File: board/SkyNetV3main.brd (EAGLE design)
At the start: 38 x 67 mm, 61 parts, among them IC1 HC_05, IC2 RF4463PRO, IC3 LPC1768, IC4 BCX17, IC5 TPS63001, IC6 MCP73871-2CCI/ML, Q1 32.768KHz, Q2 12MHz, Q3 IRLM6402, Q4 BSS138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

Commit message: corrected some distance problems and missing VALUEs
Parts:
- IC3: value LPC1768 -> LPC1769
- JP4: value (none) -> EXT
- SJ1: value (none) -> MEASURE
- moved U$1 0.28 mm to (27.5, 3.63)
- moved IC2 0.25 mm to (29.6, 14.8)
- moved JP4 0.10 mm to (34.4, 55.1)

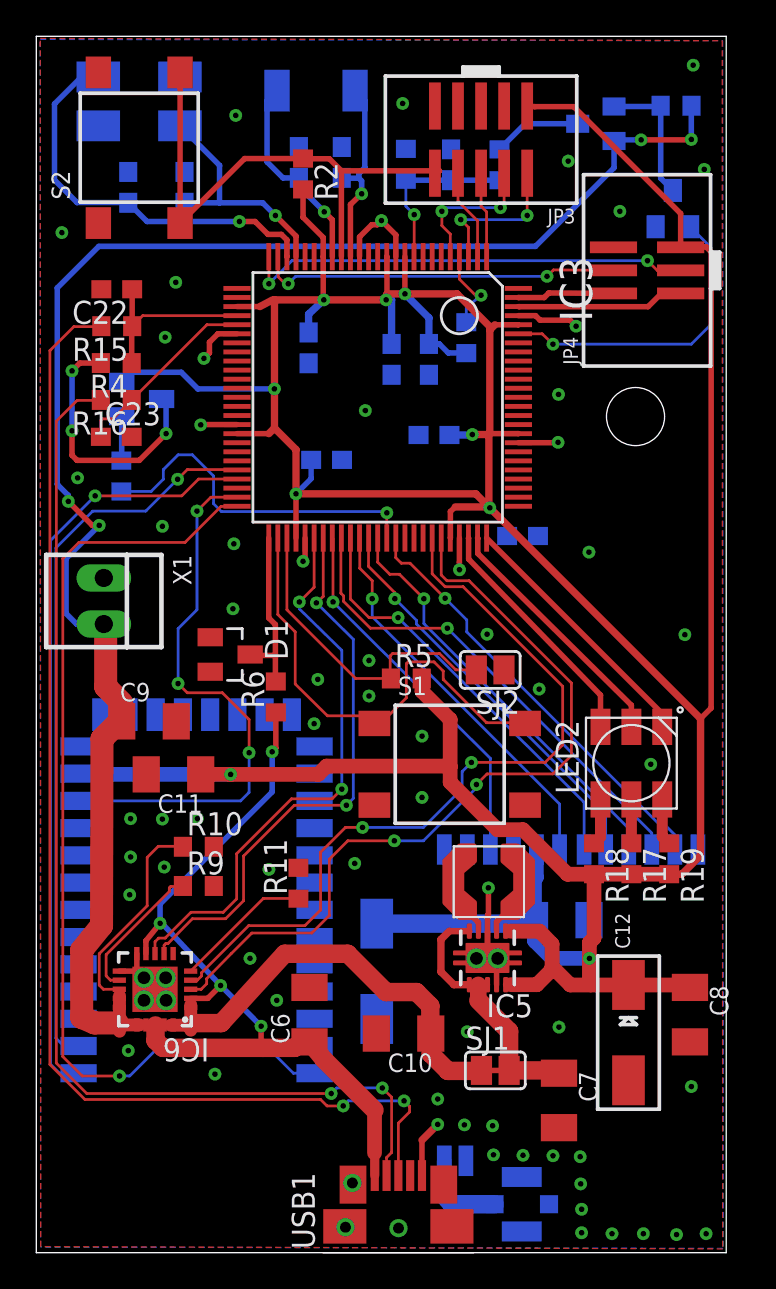
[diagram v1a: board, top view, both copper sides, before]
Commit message: layout & schematic fixes
+ layout: better ground flow
+ layout: more space for single parts
+ layout: marked GND on battery
+ layout: marked pinouts
+ schematics: fixed USB-connect->USB-plus connection
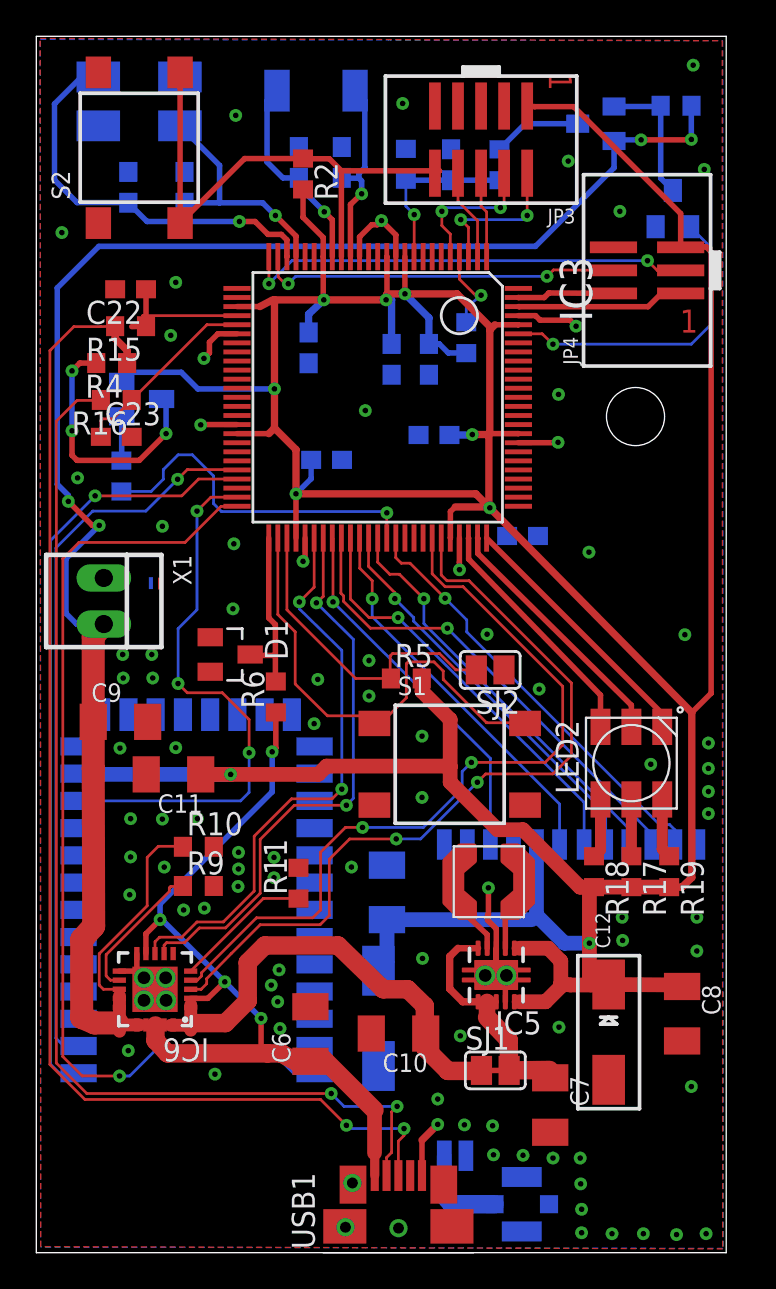
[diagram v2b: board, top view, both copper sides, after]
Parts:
- moved C1 9.75 mm to (20.1, 20.8), turned to 90 degrees
- moved C13 2.59 mm to (19.6, 13.9)
- moved C9 1.58 mm to (5.44, 30.2)
- moved C12 1.09 mm to (32.3, 13.1)
- moved C6 1.07 mm to (15.9, 13.0)
- moved IC5 1.06 mm to (26.1, 16.3)
- moved C22 0.76 mm to (5.99, 54.0)
- moved R15 0.76 mm to (5.99, 52.0)
- moved R17 0.71 mm to (33.6, 21.9)
- moved R18 0.71 mm to (31.5, 21.9)
- moved R19 0.71 mm to (35.7, 21.9)
- moved C7 0.55 mm to (29.1, 9.09)
- moved C8 0.43 mm to (36.4, 14.1)
- moved IC2 0.28 mm to (29.6, 15.1)
- moved C10 0.28 mm to (20.8, 13.0)
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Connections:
- net N$2 renamed USB-CABLE-D-
- removed net N$3: R15.2, USB1.3
- new net USB-CABLE-D+: R15.2, R4.1, USB1.3
- net USB-D+: no longer R4.1
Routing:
- net USB-CABLE-D+: track 0.00 -> 69.5 mm, vias 0 -> 2
- net N$3: track 67.8 -> 0.00 mm, vias 2 -> 0
- net USB-D+: track 10.1 -> 8.62 mm
- net VCC: track 14.6 -> 13.3 mm
- net OUT2: track 26.8 -> 28.1 mm
- net L1: track 3.24 -> 4.42 mm
- net GND: track 31.9 -> 33.1 mm, vias 73 -> 96
- net V+: track 94.6 -> 93.7 mm
- net +5V: track 49.1 -> 49.8 mm
- net LED-G-R: track 2.57 -> 3.28 mm
- net LED-R-R: track 2.42 -> 3.13 mm
- net LED-B-R: track 2.58 -> 3.29 mm
- net L2: track 3.36 -> 4.04 mm
- net +3V3: track 243.7 -> 244.3 mm
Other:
- board text added: "-"
- board text added: "1"

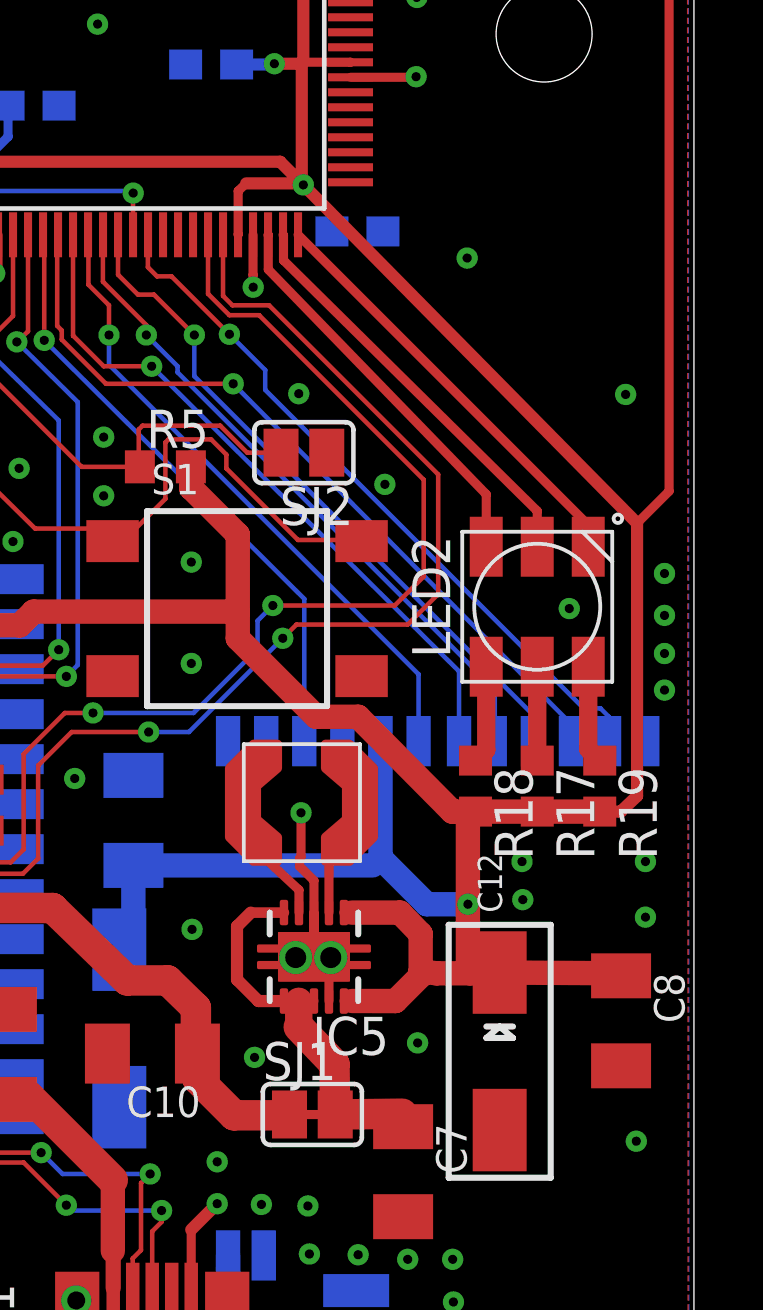
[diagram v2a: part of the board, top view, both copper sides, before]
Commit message: board: connected PS/SYNC of buck boost converter
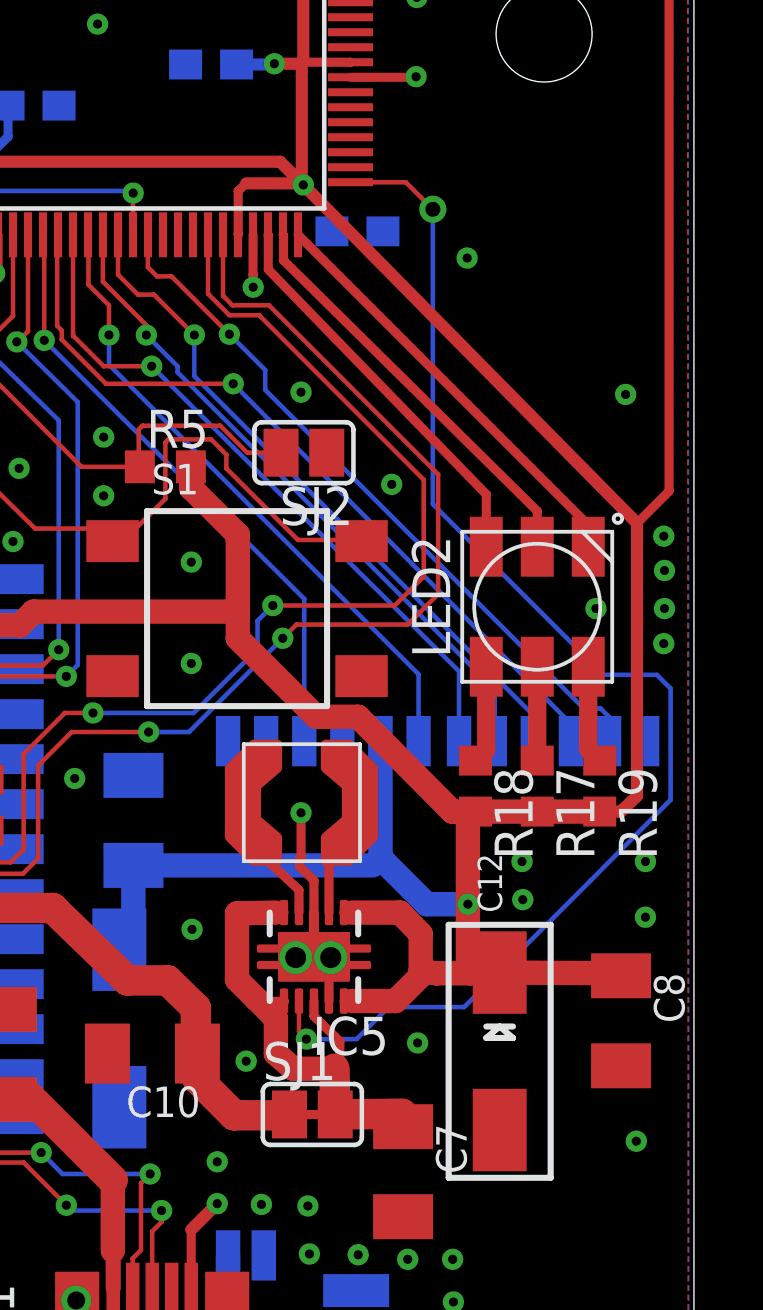
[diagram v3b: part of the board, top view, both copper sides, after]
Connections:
- new net DCDCPS: IC3.76, IC5.7
- net VCC: no longer IC5.7
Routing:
- net DCDCPS: track 0.00 -> 43.9 mm, vias 0 -> 2
- net VCC: track 13.3 -> 16.7 mm
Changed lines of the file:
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@@
 <via x="37.6936" y="2.0066" extent="1-16" drill="0.3048"/>
 <via x="22.9108" y="9.4234" extent="1-16" drill="0.3048"/>
-<via x="24.1554" y="12.9032" extent="1-16" drill="0.3048"/>
+<via x="23.876" y="12.7762" extent="1-16" drill="0.3048"/>
 <via x="13.8938" y="21.6154" extent="1-16" drill="0.3048"/>
 <via x="7.8486" y="22.1996" extent="1-16" drill="0.3048"/>
@@
 <wire x1="15.6052" y1="40.3232" x2="15.6052" y2="39.1764" width="0.3048" layer="1"/>
 <wire x1="15.6052" y1="39.1764" x2="15.494" y2="39.0398" width="0.3048" layer="1"/>
-<via x="34.6456" y="27.8638" extent="1-16" drill="0.3048"/>
-<via x="28.4988" y="32.004" extent="1-16" drill="0.3048"/>
+<via x="35.5346" y="27.8638" extent="1-16" drill="0.3048"/>
+<via x="28.7274" y="32.004" extent="1-16" drill="0.3048"/>
 <via x="7.747" y="40.9702" extent="1-16" drill="0.3048"/>
 <via x="11.684" y="40.005" extent="1-16" drill="0.3048"/>
@@
 <via x="16.1036" y="30.099" extent="1-16" drill="0.3048"/>
 <via x="19.1262" y="33.5788" extent="1-16" drill="0.3048"/>
-<via x="25.6286" y="35.0266" extent="1-16" drill="0.3048"/>
+<via x="25.7048" y="35.0774" extent="1-16" drill="0.3048"/>
 <via x="11.6332" y="36.4236" extent="1-16" drill="0.3048"/>
 <via x="25.7048" y="21.0566" extent="1-16" drill="0.3048"/>
@@
 <via x="33.0708" y="19.431" extent="1-16" drill="0.3048"/>
 <via x="33.0962" y="18.161" extent="1-16" drill="0.3048"/>
-<via x="37.8206" y="29.0322" extent="1-16" drill="0.3048"/>
-<via x="37.8206" y="27.6352" extent="1-16" drill="0.3048"/>
-<via x="37.8206" y="26.3652" extent="1-16" drill="0.3048"/>
-<via x="37.8206" y="25.146" extent="1-16" drill="0.3048"/>
+<via x="37.8206" y="29.1338" extent="1-16" drill="0.3048"/>
+<via x="37.8206" y="27.8638" extent="1-16" drill="0.3048"/>
+<via x="37.7952" y="26.6954" extent="1-16" drill="0.3048"/>
+<via x="37.7952" y="30.2768" extent="1-16" drill="0.3048"/>
 </signal>
 <signal name="RTCX1">
@@
 <contactref element="IC5" pad="8"/>
 <contactref element="IC5" pad="6"/>
-<contactref element="IC5" pad="7"/>
 <contactref element="SJ1" pad="2"/>
 <wire x1="26.8446" y1="11.0002" x2="29.0824" y2="11.0256" width="1.016" layer="1"/>
 <wire x1="29.0824" y1="11.0256" x2="29.1084" y2="10.5932" width="0.3048" layer="1"/>
-<wire x1="26.8446" y1="11.0002" x2="26.8192" y2="12.6778" width="1.016" layer="1"/>
-<wire x1="26.8192" y1="12.6778" x2="25.6286" y2="13.9192" width="1.016" layer="1"/>
-<wire x1="25.6286" y1="13.9192" x2="25.6286" y2="14.773" width="0.9144" layer="1"/>
-<wire x1="25.6286" y1="14.773" x2="25.6366" y2="14.781" width="0.3048" layer="1"/>
-<wire x1="26.1366" y1="14.781" x2="25.6366" y2="14.781" width="0.3048" layer="1"/>
-<wire x1="25.6286" y1="14.773" x2="25.1446" y2="14.773" width="0.4064" layer="1"/>
+<wire x1="26.8446" y1="11.0002" x2="26.8192" y2="12.5254" width="1.016" layer="1"/>
 <wire x1="25.1446" y1="14.773" x2="25.1366" y2="14.781" width="0.3048" layer="1"/>
-<wire x1="25.1366" y1="14.781" x2="24.2842" y2="14.781" width="0.4064" layer="1"/>
-<wire x1="24.2842" y1="14.781" x2="23.5712" y2="15.494" width="0.4064" layer="1"/>
-<wire x1="23.5712" y1="15.494" x2="23.5712" y2="17.272" width="0.4064" layer="1"/>
-<wire x1="23.5712" y1="17.272" x2="24.0284" y2="17.7292" width="0.4064" layer="1"/>
-<wire x1="24.0284" y1="17.7292" x2="25.1348" y2="17.7292" width="0.3556" layer="1"/>
-<wire x1="25.1348" y1="17.7292" x2="25.1366" y2="17.731" width="0.3048" layer="1"/>
+<wire x1="23.5712" y1="15.494" x2="23.5712" y2="17.7038" width="0.8128" layer="1"/>
+<wire x1="23.5712" y1="17.7038" x2="24.8554" y2="17.7292" width="0.8128" layer="1"/>
+<wire x1="24.8554" y1="17.7292" x2="25.1366" y2="17.731" width="0.3048" layer="1"/>
+<wire x1="26.8192" y1="12.5254" x2="25.4476" y2="12.5254" width="0.8128" layer="1"/>
+<wire x1="25.4476" y1="12.5254" x2="24.8666" y2="13.0302" width="0.8128" layer="1"/>
+<wire x1="24.8666" y1="13.0302" x2="24.8666" y2="14.1986" width="0.8128" layer="1"/>
+<wire x1="24.8666" y1="14.1986" x2="24.2189" y2="14.8463" width="0.8128" layer="1"/>
+<wire x1="24.2189" y1="14.8463" x2="23.5712" y2="15.494" width="0.8128" layer="1"/>
+<wire x1="25.1446" y1="14.773" x2="24.2922" y2="14.773" width="0.3048" layer="1"/>
+<wire x1="24.2922" y1="14.773" x2="24.2189" y2="14.8463" width="0.3048" layer="1"/>
+<wire x1="26.1366" y1="14.781" x2="26.1366" y2="14.2748" width="0.3048" layer="1"/>
+<wire x1="26.1366" y1="14.2748" x2="27.0002" y2="13.4366" width="0.3048" layer="1"/>
+<wire x1="27.0002" y1="13.4366" x2="27.0002" y2="12.8588" width="0.3048" layer="1"/>
+<wire x1="27.0002" y1="12.8588" x2="26.8192" y2="12.5254" width="0.3048" layer="1"/>
 </signal>
 <signal name="V+">
@@
 <wire x1="5.1435" y1="51.9929" x2="5.1444" y2="51.9938" width="0.4064" layer="1"/>
 </signal>
+<signal name="DCDCPS">
+<contactref element="IC3" pad="76"/>
+<contactref element="IC5" pad="7"/>
+<wire x1="25.6366" y1="14.781" x2="25.6366" y2="13.7588" width="0.1524" layer="1"/>
+<wire x1="25.6366" y1="13.7588" x2="25.8826" y2="13.5128" width="0.1524" layer="1"/>
+<via x="25.8826" y="13.5128" extent="1-16" drill="0.3048"/>
+<wire x1="25.8826" y1="13.5128" x2="27.559" y2="13.5128" width="0.1524" layer="16"/>
+<wire x1="27.3552" y1="42.0732" x2="29.1992" y2="42.0732" width="0.1524" layer="1"/>
+<wire x1="29.1992" y1="42.0732" x2="30.099" y2="41.1734" width="0.1524" layer="1"/>
+<via x="30.099" y="41.1734" extent="1-16" drill="0.5"/>
+<wire x1="30.099" y1="41.1734" x2="30.099" y2="31.3436" width="0.1524" layer="16"/>
+<wire x1="30.099" y1="31.3436" x2="35.7886" y2="25.654" width="0.1524" layer="16"/>
+<wire x1="35.7886" y1="25.654" x2="37.5666" y2="25.654" width="0.1524" layer="16"/>
+<wire x1="31.1404" y1="14.5796" x2="28.6258" y2="14.5796" width="0.1524" layer="16"/>
+<wire x1="28.6258" y1="14.5796" x2="27.559" y2="13.5128" width="0.1524" layer="16"/>
+<wire x1="37.5666" y1="25.654" x2="38.0238" y2="25.1968" width="0.1524" layer="16"/>
+<wire x1="38.0238" y1="25.1968" x2="38.0238" y2="21.4884" width="0.1524" layer="16"/>
+<wire x1="38.0238" y1="21.4884" x2="35.3568" y2="18.796" width="0.1524" layer="16"/>
+<wire x1="35.3568" y1="18.796" x2="31.1404" y2="14.5796" width="0.1524" layer="16"/>
+</signal>
 </signals>
